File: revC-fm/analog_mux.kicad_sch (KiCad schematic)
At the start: 33 parts, among them J2 T1M-08-F-SV-L, U16 74HC4067PW,118, U17 OPA340MDBVTEP

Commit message: working revC
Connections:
- net BATT_NTC: no longer names the net of U16.5 (I4)
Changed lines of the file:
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@@
-    )
-  )
-  (global_label "BATT_NTC" (shape input) (at 181.61 82.55 0) (fields_autoplaced)
-    (effects (font (size 1.27 1.27)) (justify left))
-    (property "Intersheetrefs" "${INTERSHEET_REFS}" (at 192.7637 82.4706 0)
-      (effects (font (size 1.27 1.27)) (justify left) hide)
     )
   )

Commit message: working revC
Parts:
- renumbered C60 to C49, C59 to C50, R113 to R100, R123 to R101, R125 to R102, R106 to R103, R114 to R104, R124 to R105, R126 to R106, R107 to R79, R115 to R80, R121 to R81, R108 to R82, R116 to R83, R122 to R84, R134 to R85, R127 to R86, R128 to R87, R129 to R88, R109 to R89, R111 to R90, R117 to R91, R119 to R92, R130 to R93, R131 to R94, R110 to R95, R112 to R96, R118 to R97, R120 to R98, R105 to R99, U17 to U10, U16 to U11
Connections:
- no-connect marks 1 -> 2

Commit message: working revC
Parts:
- removed J2: T1M-08-F-SV-L, mainboard-SLI:SAMTEC_T1M-08-F-SV-L, symbol Connector_Generic:Conn_02x04_Odd_Even
- removed R79, R80, R81, R82, R83: 100k, Resistor_SMD:R_0603_1608Metric, symbol Device:R_US
- removed R84, R89, R90, R91, R92: 10k, Resistor_SMD:R_0603_1608Metric, symbol Device:R_US
- added R28, R29, R30, R31: 10k, Resistor_SMD:R_0603_1608Metric, symbol Device:R_US
- renumbered C49 to C27, C50 to C28, R85 to R32, R86 to R33, R87 to R34, R88 to R35, R93 to R40, R94 to R41, R95 to R42, R96 to R43, R97 to R44, R98 to R45, R99 to R46, R100 to R47, R101 to R48, R102 to R49, R103 to R50, R104 to R51, R105 to R52, R106 to R53, U10 to U8, U11 to U9
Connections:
- net NTC2 is gone; now on net ADD_TEMP_1: U9.22 (I9)
- net NTC3 is gone; now on net ADD_TEMP_1: U9.21 (I10)
- net NTC4 is gone; now on net ADD_TEMP_1: U9.20 (I11)
- net VRF_NTC is gone; now on net ADD_TEMP_1: U9.2 (I7)
- net 3.3V: now also R28.1, R29.1, R30.1, R31.1
- net CHRG_TEMP: now reaches U9.5 (I4)
- net BUS_NTC1: now reaches U9.9 (I0)
- net BUS_NTC1: now also R31.2
- net NTC1 renamed ADD_TEMP_1
- net SLR_CHRG_NTC renamed PYLD_REG_TEMP
- net VPYLD_NTC renamed RF_REG_TEMP
- net VSOLAR_adc renamed BUS_NTC4
- net BUS_NTC4: now also R28.2
- net Vcc_PYLD_adc renamed BUS_NTC2
- net BUS_NTC2: now also R30.2
- net Vcc_RF_adc renamed BUS_NTC3
- net BUS_NTC3: now also R29.2
- net slr_temp_1 renamed SOLAR_TEMP_1
- net slr_temp_2 renamed SOLAR_TEMP_2
- net slr_temp_3 renamed SOLAR_TEMP_3
- net slr_temp_4 renamed SOLAR_TEMP_4
- no-connect marks 2 -> 0
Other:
- note added: "revaualuate this design choice!!!"
- moved on the sheet: C27, C28, R32, R33, R34, R35, R40, R41, R42, R43, R44, R45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

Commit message: routing fm
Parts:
- removed C27: 0.1uF, Capacitor_SMD:C_0603_1608Metric, symbol Device:C
- removed R28, R29, R30, R31: 10k, Resistor_SMD:R_0603_1608Metric, symbol Device:R_US
- removed R33, R34, R35, R40, R42, R43, R44, R45: 1k, Resistor_SMD:R_0603_1608Metric, symbol Device:R_US
- removed R46, R47, R48, R49, R50, R51, R52, R53: 100k, Resistor_SMD:R_0603_1608Metric, symbol Device:R_US
- removed U8: OPA340MDBVTEP, Package_TO_SOT_SMD:SOT-23-5, symbol Amplifier_Operational:OPA340NA
- added C119: 0.1uF, Capacitor_SMD:C_0603_1608Metric, symbol Device:C
- added RN1 (x2): 1k, SierraLobo:RAVF164D, symbol SierraLobo:R_Network04_US
- added U35: LT6004CMS8#PBF, Package_SO:MSOP-8_3x3mm_P0.65mm, symbol SierraLobo:LT6004CMS8#PBF
- added U37: DG4052EEN-T1-GE4, symbol SierraLobo:DG4052EEN-T1-GE4
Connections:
- net 3.3V: now also C119.1, U37.14 (V+)
- net GND: now also C119.2
- net MUX_S0: now also RN1.6
- net MUX_S1: now also RN1.5
- net MUX_S2: now also RN1.7
- net MUX_S3: now also RN1.8
- net SLR_TLE_1: now also U37.10 (X0)
- net SLR_TLE_2: now also U37.12 (X1)
- net SLR_TLE_3: now also U37.13 (X2)
- net SLR_TLE_4: now also U37.9 (X3)
- net mux_out: now also U35.5 (+)
- net at U9.10 (S0): now also RN1.3
- net at U9.13 (S3): now also RN1.1
- net at U9.14 (S2): now also RN1.2
- net at U9.11 (S1): now also RN1.4
- net at R32.1: now also U35.6 (-), U35.7
- removed net ADD_TEMP_1: U9.2 (I7), U9.20 (I11), U9.21 (I10), U9.22 (I9), U9.23 (I8)
- net AIN5 renamed AMUX
- net BUS_NTC1 renamed TLE_MUX
- net BUS_NTC2 renamed NTC_MUX
- net BUS_NTC3 renamed TEMP_A
- net BUS_NTC4 renamed TEMP_B
- net CHRG_TEMP renamed TEMP_C
- net PYLD_REG_TEMP renamed TEMP_D
- net RF_REG_TEMP renamed TEMP_E
- net SOLAR_TEMP_1: no longer names the net of U9.19 (I12)
- net SOLAR_TEMP_2: no longer names the net of U9.18 (I13)
- net SOLAR_TEMP_3: no longer names the net of U9.17 (I14)
- net SOLAR_TEMP_4: no longer names the net of U9.16 (I15)
- net ~{MUX_EN} renamed ~{MUX_EN1}
- new net: RN1.5, U37.8 (A)
- new net: RN1.6, U37.7 (B)
- new net: RN1.7, U37.4 (EN)
- new net MUX_A: RN1.4
- new net MUX_B: RN1.3
- new net MUX_EN2: RN1.2
- new net NTC: U37.1 (Y)
- new net NTC1: U37.15 (Y0)
- new net NTC2: U37.3 (Y1)
- new net NTC3: U37.16 (Y2)
- new net NTC4: U37.2 (Y3)
- new net PIB_TEMP_1: U9.23 (I8)
- new net PIB_TEMP_2: U9.22 (I9)
- new net PIB_TEMP_3: U9.21 (I10)
- new net PIB_TEMP_4: U9.20 (I11)
- new net TEMP_F: U9.2 (I7)
- new net TLE: U37.11 (X)
- no-connect marks 0 -> 4
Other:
- added sheet NTC Signal Conditioning (ntc_cond.kicad_sch)
- added sheet Solar TLE Conditioning (tle_cond.kicad_sch)
- note removed: "lm355a is rated to 100degC arbitrarily selecting max temp sensed as 400K ~ 125C"
- note removed: "really should have an op amp here but board space is already constrained"
- note removed: "revaualuate this design choice!!!"
- moved on the sheet: C28, R32, R41, U9

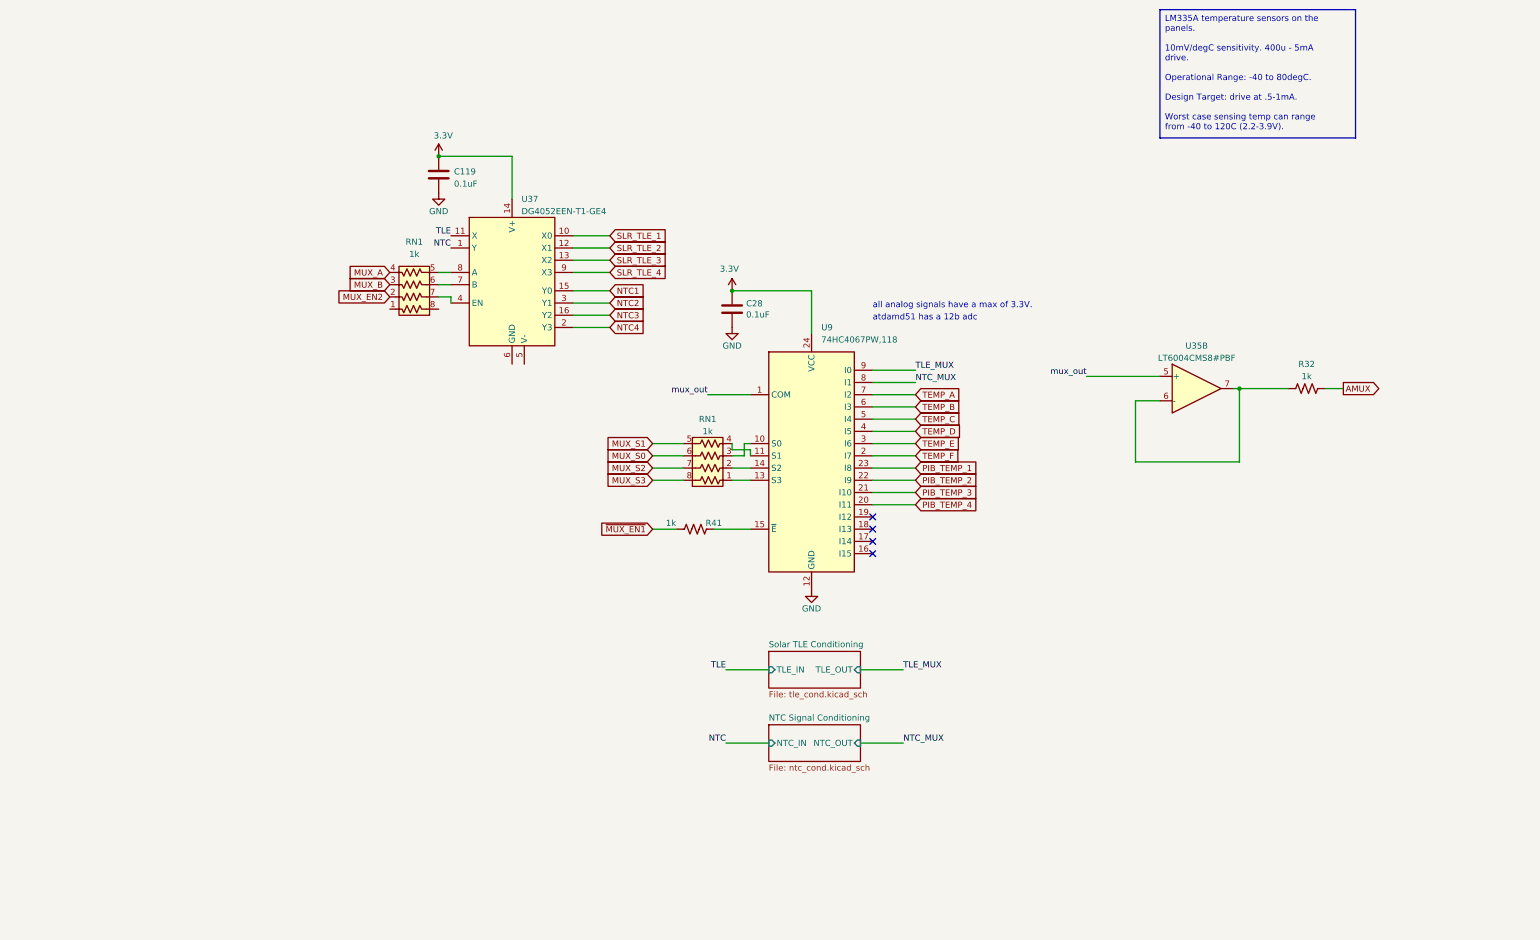
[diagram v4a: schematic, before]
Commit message: updated analog , solar comp, layout
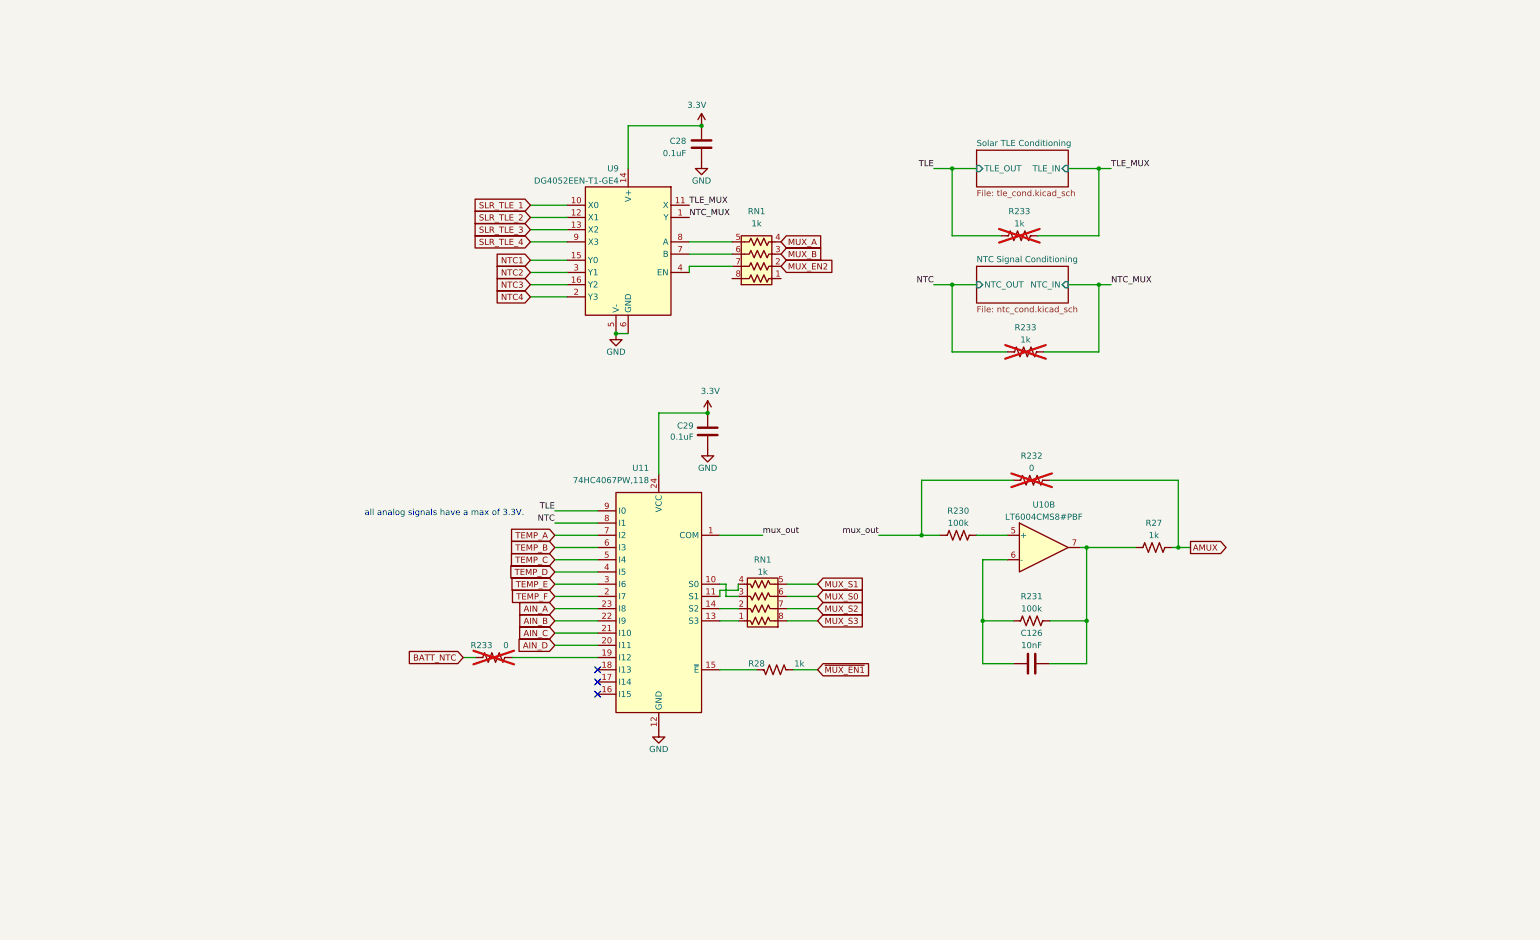
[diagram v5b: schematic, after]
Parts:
- added C126: 10nF, symbol Device:C
- added R230, R231: 100k, symbol Device:R_US
- added R232, R233: 0, Resistor_SMD:R_0603_1608Metric, symbol Device:R_US
- added R233 (x2): 1k, Resistor_SMD:R_0603_1608Metric, symbol Device:R_US
- renumbered C119 to C28, C28 to C29, R32 to R27, R41 to R28, U35 to U10, U9 to U11, U37 to U9
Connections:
- net AMUX: now also R232.2
- net GND: now also U9.5 (V-), U9.6 (GND)
- net NTC: now also U11.8 (I1), R233.1; no longer U9.1 (Y)
- net NTC_MUX: now also U9.1 (Y), R233.2; no longer U11.8 (I1)
- net TLE: now also U11.9 (I0), R233.1; no longer U9.11 (X)
- net TLE_MUX: now also U9.11 (X), R233.2; no longer U11.9 (I0)
- net mux_out: now also R230.1, R232.1; no longer U10.5 (+)
- net at R27.1, U10.7: now also C126.2, R231.2; no longer U10.6 (-)
- net at U11.19 (I12): now also R233.2
- net PIB_TEMP_1 renamed AIN_A
- net PIB_TEMP_2 renamed AIN_B
- net PIB_TEMP_3 renamed AIN_C
- net PIB_TEMP_4 renamed AIN_D
- new net: C126.1, R231.1, U10.6 (-)
- new net: R230.2, U10.5 (+)
- new net BATT_NTC: R233.1
- no-connect marks 4 -> 3
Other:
- note removed: "atdamd51 has a 12b adc"
- moved on the sheet: C28, C29, R27, R28, RN1, U10B, U11, U9
